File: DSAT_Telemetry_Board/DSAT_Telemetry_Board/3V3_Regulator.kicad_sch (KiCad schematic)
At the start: 5 parts

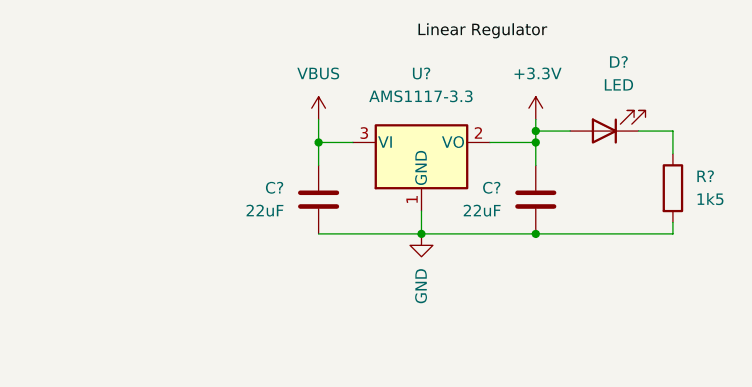
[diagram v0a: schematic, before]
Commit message: Seperate Branch
Updated Pin names, Added LNA, Fixed Pins on USB connection
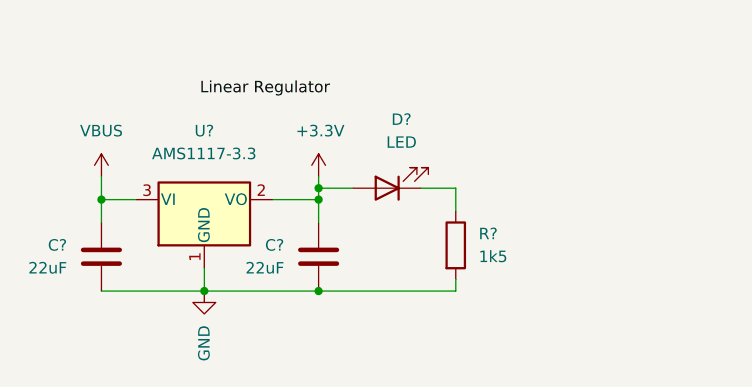
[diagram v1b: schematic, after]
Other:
- moved on the sheet: C?, D?, R?, U?
